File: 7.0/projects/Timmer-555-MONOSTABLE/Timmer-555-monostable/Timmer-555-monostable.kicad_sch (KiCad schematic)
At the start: 0 parts

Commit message: adding 555 monostable
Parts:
- added C1: C_Polarized, symbol Device:C_Polarized
- added D1: LED, LED_THT:LED_D5.0mm, symbol Device:LED
- added RA1, Rp1: 10k, Resistor_THT:R_Axial_DIN0207_L6.3mm_D2.5mm_P7.62mm_Horizontal, symbol Device:R
- added RL1: 220, Resistor_THT:R_Axial_DIN0207_L6.3mm_D2.5mm_P7.62mm_Horizontal, symbol Device:R
- added SOURCE_VCC1: 5, Connector_AMASS:AMASS_XT30U-M_1x02_P5.0mm_Vertical, symbol Simulation_SPICE:VDC
- added SW0: SW_SWITCH, TerminalBlock:TerminalBlock_bornier-3_P5.08mm, symbol Switch:SW_SPDT_321
- added SW1: SW_Push, Button_Switch_THT:SW_PUSH_6mm_H5mm, symbol Switch:SW_Push
- added U1: LM555xM, Package_DIP:DIP-8_W7.62mm_Socket_LongPads, symbol Timer:LM555xM
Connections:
- new net: RL1.1, U1.3 (Q)
- new net: RA1.1, Rp1.1, SW0.1 (C), U1.8 (VCC)
- new net: D1.2 (A), RL1.2
- new net: SOURCE_VCC1.1, SW0.2 (B)
- new net GND: C1.2, D1.1 (K), SOURCE_VCC1.2, SW1.1, U1.1 (GND)
- new net THR: C1.1, RA1.2, U1.6 (THR), U1.7 (DIS)
- new net TRG: Rp1.2, SW1.2, U1.2 (TR)

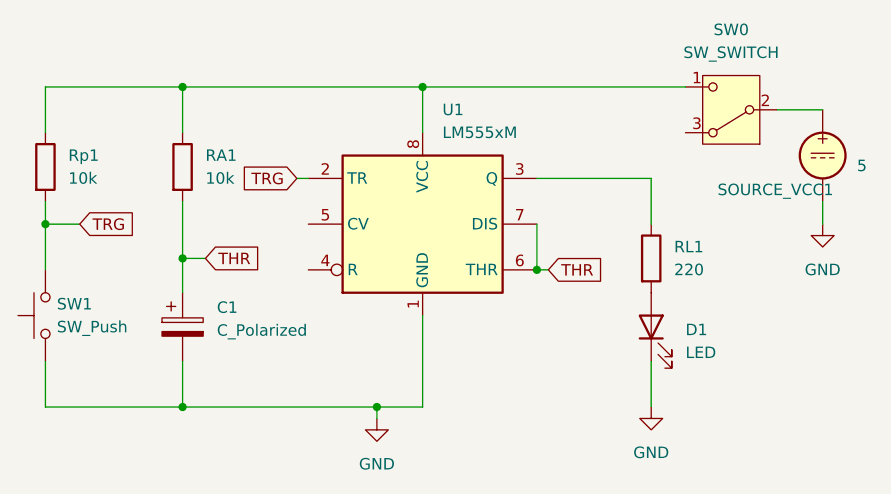
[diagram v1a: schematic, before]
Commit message: adding 555-monostable ok
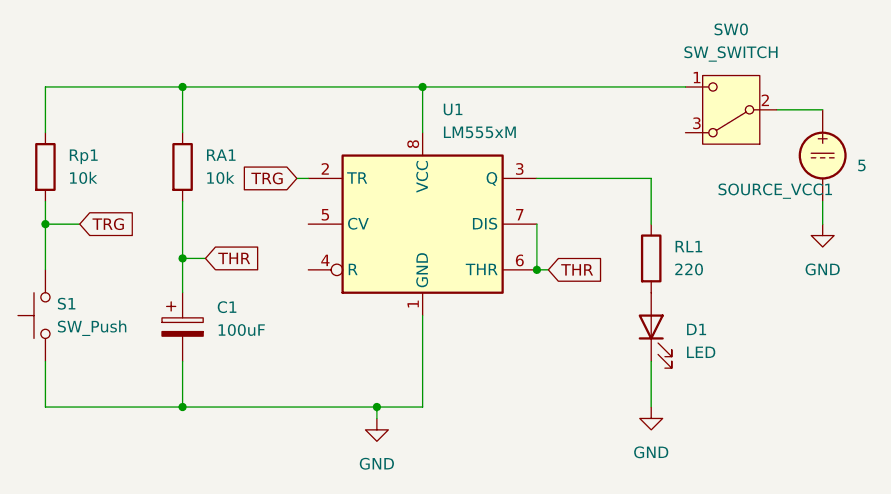
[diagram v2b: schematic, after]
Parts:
- C1: value C_Polarized -> 100uF; footprint (none) -> Capacitor_THT:CP_Radial_D10.0mm_P7.50mm
- SW0: footprint TerminalBlock:TerminalBlock_bornier-3_P5.08mm -> TerminalBlock:TerminalBlock_MaiXu_MX126-5.0-03P_1x03_P5.00mm
- renumbered SW1 to S1
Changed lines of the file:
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@@
 			)
 		)
-		(property "Footprint" "TerminalBlock:TerminalBlock_bornier-3_P5.08mm"
+		(property "Footprint" "TerminalBlock:TerminalBlock_MaiXu_MX126-5.0-03P_1x03_P5.00mm"
 			(at 144.78 59.69 0)
 			(effects
@@
 			)
 		)
-		(property "Value" "C_Polarized"
+		(property "Value" "100uF"
 			(at 87.63 94.3609 0)
 			(effects
@@
 			)
 		)
-		(property "Footprint" ""
+		(property "Footprint" "Capacitor_THT:CP_Radial_D10.0mm_P7.50mm"
 			(at 84.7852 97.79 0)
 			(effects
@@
 		(dnp no)
 		(fields_autoplaced yes)
-		(property "Reference" "SW1"
+		(property "Reference" "S1"
 			(at 69.85 91.4399 90)
 			(effects
@@
 			(project "Timmer-555-monostable"
 				(path "/e06b5055-5c54-40fd-b79f-9ceb966d6c9b"
-					(reference "SW1")
-					(unit 1)
-				)
+					(reference "S1")
+					(unit 1)
+				)

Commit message: adding goog values for 555 project
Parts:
- C1: value 100uF -> 270uF
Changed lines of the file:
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@@
 			)
 		)
-		(property "Value" "100uF"
+		(property "Value" "270uF"
 			(at 87.63 94.3609 0)
 			(effects
